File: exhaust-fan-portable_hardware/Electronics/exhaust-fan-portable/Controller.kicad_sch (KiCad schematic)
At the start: 4 parts, among them SW1 SW_Push, SW2 SW_Push, U1 ESP32-S3-WROOM-2

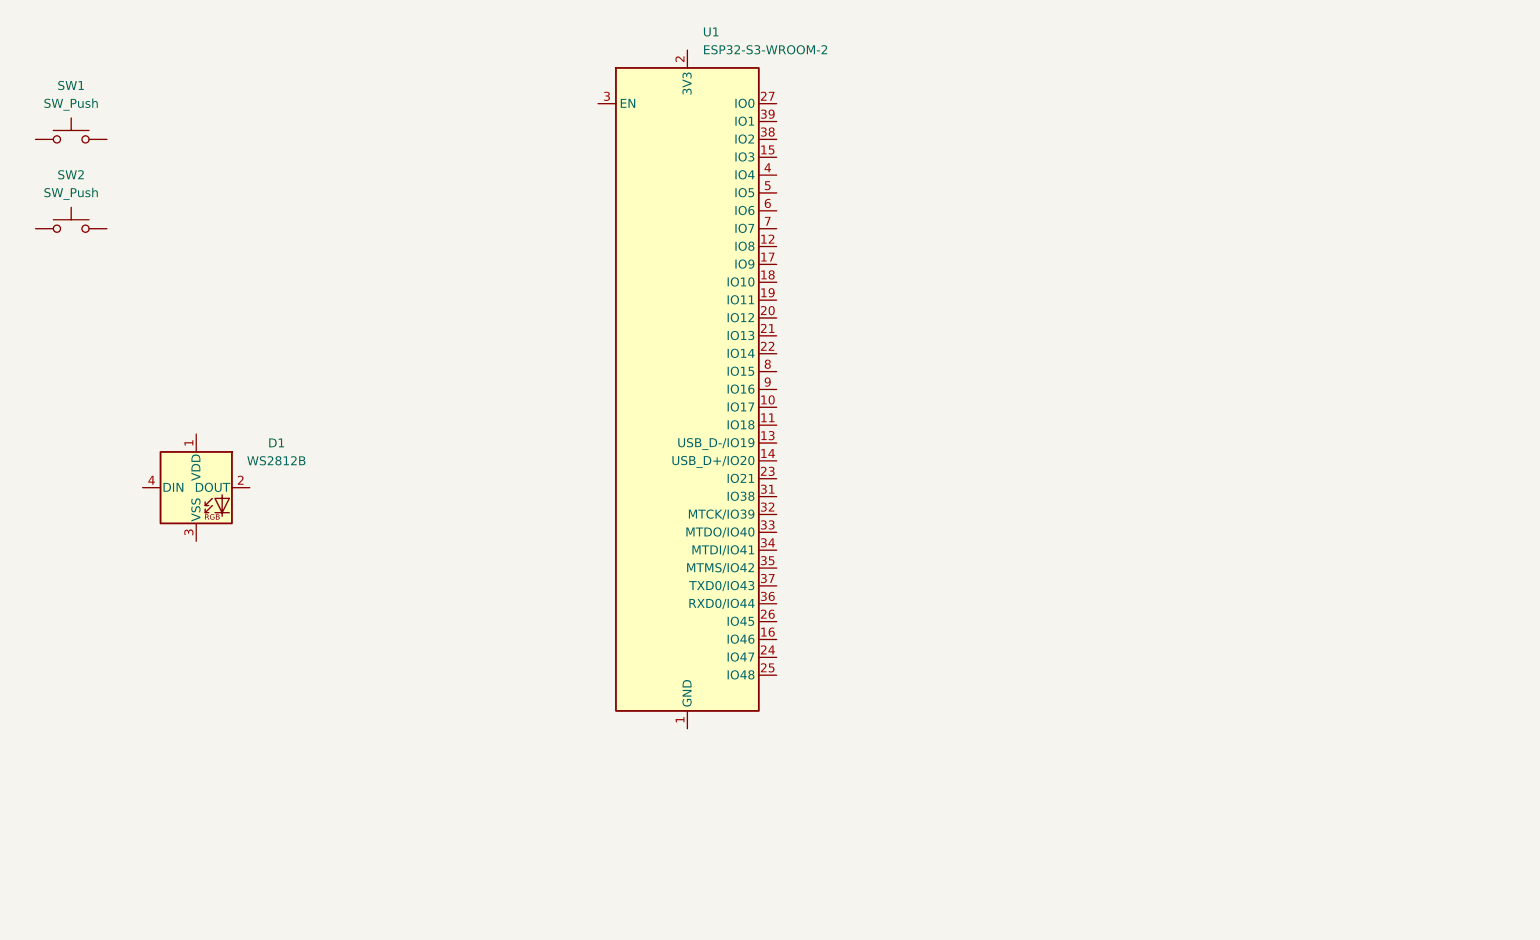
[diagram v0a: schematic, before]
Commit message: layed out rough schematic and added sensor comparison
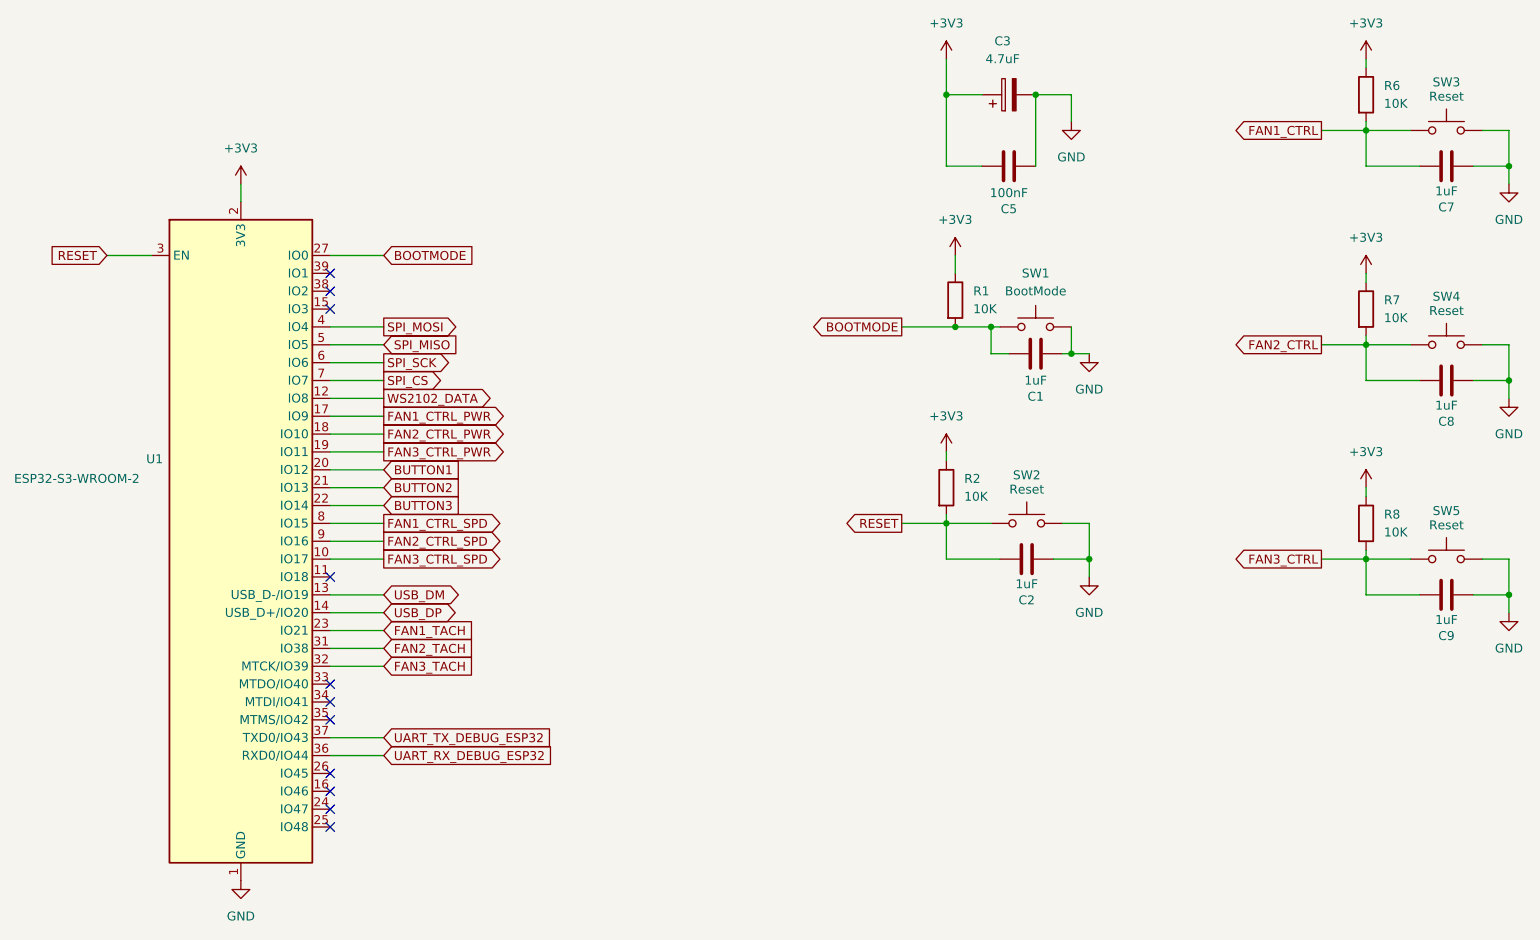
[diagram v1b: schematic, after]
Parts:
- removed D1: WS2812B, LED_SMD:LED_WS2812B_PLCC4_5.0x5.0mm_P3.2mm, symbol LED:WS2812B
- added C1, C2, C7, C8, C9: 1uF, symbol Device:C
- added C3: 4.7uF, symbol Device:C_Polarized
- added C5: 100nF, symbol Device:C
- added R1, R2, R6, R7, R8: 10K, symbol Device:R
- added SW3, SW4, SW5: Reset, symbol Switch:SW_Push
- SW1: value SW_Push -> BootMode
- SW2: value SW_Push -> Reset
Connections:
- net GND: now reaches SW2.1
- net GND: now also SW1.2, U1.1 (GND), U1.40 (GND), U1.41 (GND), C1.2, C2.1, C3.2, C5.2, C7.1, C8.1, C9.1, SW3.1, SW4.1, SW5.1
- net RESET: now reaches SW2.2
- net RESET: now also U1.3 (EN), C2.2, R2.2
- net BOOTMODE: now reaches SW1.1
- net BOOTMODE: now also U1.27 (IO0), C1.1, R1.2
- net FAN3_CTRL_SPD: now reaches U1.10 (IO17)
- net WS2102_DATA: now reaches U1.12 (IO8)
- net USB_DM: now reaches U1.13 (USB_D-/IO19)
- net USB_DP: now reaches U1.14 (USB_D+/IO20)
- net FAN1_CTRL_PWR: now reaches U1.17 (IO9)
- net FAN2_CTRL_PWR: now reaches U1.18 (IO10)
- net FAN3_CTRL_PWR: now reaches U1.19 (IO11)
- net +3V3: now reaches U1.2 (3V3)
- net +3V3: now also C3.1, C5.1, R1.1, R2.1, R6.1, R7.1, R8.1
- net BUTTON1: now reaches U1.20 (IO12)
- net BUTTON2: now reaches U1.21 (IO13)
- net BUTTON3: now reaches U1.22 (IO14)
- net FAN1_TACH: now reaches U1.23 (IO21)
- net FAN2_TACH: now reaches U1.31 (IO38)
- net FAN3_TACH: now reaches U1.32 (MTCK/IO39)
- net UART_RX_DEBUG_ESP32: now reaches U1.36 (RXD0/IO44)
- net UART_TX_DEBUG_ESP32: now reaches U1.37 (TXD0/IO43)
- net SPI_MOSI: now reaches U1.4 (IO4)
- net SPI_MISO: now reaches U1.5 (IO5)
- net SPI_SCK: now reaches U1.6 (IO6)
- net SPI_CS: now reaches U1.7 (IO7)
- net FAN1_CTRL_SPD: now reaches U1.8 (IO15)
- net FAN2_CTRL_SPD: now reaches U1.9 (IO16)
- new net FAN1_CTRL: C7.2, R6.2, SW3.2
- new net FAN2_CTRL: C8.2, R7.2, SW4.2
- new net FAN3_CTRL: C9.2, R8.2, SW5.2
- no-connect marks 0 -> 11
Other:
- moved on the sheet: SW1, SW2, U1

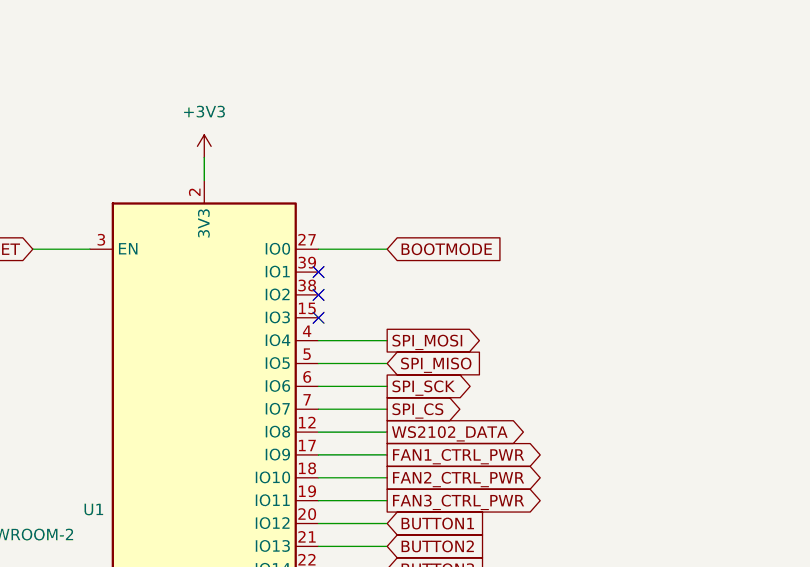
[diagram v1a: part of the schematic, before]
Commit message: fixed case design
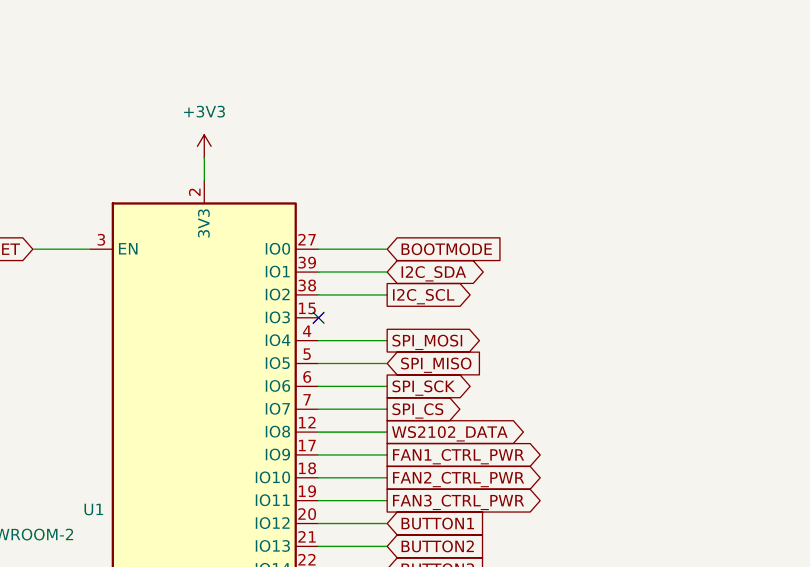
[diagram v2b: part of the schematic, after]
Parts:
- C1, C2, C7, C8, C9: footprint (none) -> Capacitor_SMD:C_0805_2012Metric_Pad1.18x1.45mm_HandSolder
- C3: footprint (none) -> Capacitor_SMD:C_1206_3216Metric_Pad1.33x1.80mm_HandSolder
- C5: footprint (none) -> Capacitor_SMD:C_0603_1608Metric_Pad1.08x0.95mm_HandSolder
- R1, R2, R6, R7, R8: footprint (none) -> Resistor_SMD:R_0603_1608Metric_Pad0.98x0.95mm_HandSolder
- SW1, SW2, SW3, SW4, SW5: footprint (none) -> Button_Switch_SMD:SW_Push_SPST_NO_Alps_SKRK
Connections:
- net I2C_SCL: now reaches U1.38 (IO2)
- net I2C_SDA: now reaches U1.39 (IO1)
- no-connect marks 11 -> 9
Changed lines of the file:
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@@
 	)
 	(no_connect
-		(at 76.2 73.66)
-	)
-	(no_connect
 		(at 76.2 78.74)
 	)
@@
 	)
 	(no_connect
-		(at 76.2 76.2)
-	)
-	(no_connect
 		(at 76.2 137.16)
 	)
@@
 	(wire
 		(pts
+			(xy 83.82 73.66) (xy 76.2 73.66)
+		)
+		(stroke
+			(width 0)
+			(type default)
+		)
+	)
+	(wire
+		(pts
 			(xy 163.83 114.3) (xy 171.45 114.3)
 		)
@@
 	(wire
 		(pts
+			(xy 83.82 76.2) (xy 76.2 76.2)
+		)
+		(stroke
+			(width 0)
+			(type default)
+		)
+	)
+	(wire
+		(pts
 			(xy 83.82 93.98) (xy 76.2 93.98)
 		)
@@
 		)
 	)
+	(global_label "I2C_SCL"
+		(shape output)
+		(at 83.82 76.2 0)
+		(fields_autoplaced yes)
+		(effects
+			(font
+				(size 1.27 1.27)
+			)
+			(justify left)
+		)
+		(property "Intersheetrefs" "${INTERSHEET_REFS}"
+			(at 94.3647 76.2 0)
+			(effects
+				(font
+					(size 1.27 1.27)
+				)
+				(justify left)
+				(hide yes)
+			)
+		)
+	)
 	(global_label "BUTTON3"
 		(shape input)
@@
 		)
 	)
+	(global_label "I2C_SDA"
+		(shape tri_state)
+		(at 83.82 73.66 0)
+		(fields_autoplaced yes)
+		(effects
+			(font
+				(size 1.27 1.27)
+			)
+			(justify left)
+		)
+		(property "Intersheetrefs" "${INTERSHEET_REFS}"
+			(at 95.5365 73.66 0)
+			(effects
+				(font
+					(size 1.27 1.27)
+				)
+				(justify left)
+				(hide yes)
+			)
+		)
+	)
 	(global_label "USB_DM"
 		(shape bidirectional)
@@
 			)
 		)
-		(property "Footprint" ""
+		(property "Footprint" "Capacitor_SMD:C_0805_2012Metric_Pad1.18x1.45mm_HandSolder"
 			(at 171.45 115.2652 0)
 			(effects
@@
 			)
 		)
-		(property "Footprint" ""
+		(property "Footprint" "Button_Switch_SMD:SW_Push_SPST_NO_Alps_SKRK"
 			(at 175.26 104.14 0)
 			(effects
@@
 			)
 		)
-		(property "Footprint" ""
+		(property "Footprint" "Button_Switch_SMD:SW_Push_SPST_NO_Alps_SKRK"
 			(at 234.95 78.74 0)
 			(effects
@@
 			)
 		)
-		(property "Footprint" ""
+		(property "Footprint" "Capacitor_SMD:C_0805_2012Metric_Pad1.18x1.45mm_HandSolder"
 			(at 180.34 84.1248 0)
 			(effects
@@
 			)
 		)
-		(property "Footprint" ""
+		(property "Footprint" "Capacitor_SMD:C_0805_2012Metric_Pad1.18x1.45mm_HandSolder"
 			(at 231.14 59.3852 0)
 			(effects
@@
 			)
 		)
-		(property "Footprint" ""
+		(property "Footprint" "Resistor_SMD:R_0603_1608Metric_Pad0.98x0.95mm_HandSolder"
 			(at 163.322 77.47 90)
 			(effects
@@
 			)
 		)
-		(property "Footprint" ""
+		(property "Footprint" "Resistor_SMD:R_0603_1608Metric_Pad0.98x0.95mm_HandSolder"
 			(at 221.742 109.22 90)
 			(effects
@@
 			)
 		)
-		(property "Footprint" ""
+		(property "Footprint" "Button_Switch_SMD:SW_Push_SPST_NO_Alps_SKRK"
 			(at 234.95 48.26 0)
 			(effects
@@
 			)
 		)
-		(property "Footprint" ""
+		(property "Footprint" "Capacitor_SMD:C_1206_3216Metric_Pad1.33x1.80mm_HandSolder"
 			(at 176.53 47.2948 0)
 			(effects
@@
 			)
 		)
-		(property "Footprint" ""
+		(property "Footprint" "Button_Switch_SMD:SW_Push_SPST_NO_Alps_SKRK"
 			(at 234.95 109.22 0)
 			(effects
@@
 			)
 		)
-		(property "Footprint" ""
+		(property "Footprint" "Resistor_SMD:R_0603_1608Metric_Pad0.98x0.95mm_HandSolder"
 			(at 221.742 48.26 90)
 			(effects
@@
 			)
 		)
-		(property "Footprint" ""
+		(property "Footprint" "Button_Switch_SMD:SW_Push_SPST_NO_Alps_SKRK"
 			(at 176.53 76.2 0)
 			(effects
@@
 			)
 		)
-		(property "Footprint" ""
+		(property "Footprint" "Capacitor_SMD:C_0805_2012Metric_Pad1.18x1.45mm_HandSolder"
 			(at 231.14 120.3452 0)
 			(effects
@@
 			)
 		)
-		(property "Footprint" ""
+		(property "Footprint" "Capacitor_SMD:C_0603_1608Metric_Pad1.08x0.95mm_HandSolder"
 			(at 176.53 57.4548 0)
 			(effects
@@
 			)
 		)
-		(property "Footprint" ""
+		(property "Footprint" "Capacitor_SMD:C_0805_2012Metric_Pad1.18x1.45mm_HandSolder"
 			(at 231.14 89.8652 0)
 			(effects
@@
 			)
 		)
-		(property "Footprint" ""
+		(property "Footprint" "Resistor_SMD:R_0603_1608Metric_Pad0.98x0.95mm_HandSolder"
 			(at 162.052 104.14 90)
 			(effects
@@
 			)
 		)
-		(property "Footprint" ""
+		(property "Footprint" "Resistor_SMD:R_0603_1608Metric_Pad0.98x0.95mm_HandSolder"
 			(at 221.742 78.74 90)
 			(effects
